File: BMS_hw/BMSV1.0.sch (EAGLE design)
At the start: 237 parts, among them IC1 MC33771BEP, IC2 SFH6156, IC3 MIC28515V1, IC4 FOD8384-COC, IC5 FOD8384-COC, IC6 FOD8384-COC, J2 NTC, Q1 IRLML5203, Q2 IRLML5203, T1 IPT020N10N3V1, T2 IPT020N10N3V1, T3 IPT020N10N3V1, T4 IPT020N10N3V1, X1 87758-2016, X2 87758-1816, X3 22-23-2041, X4 87758-2016, X5 22-23-2051

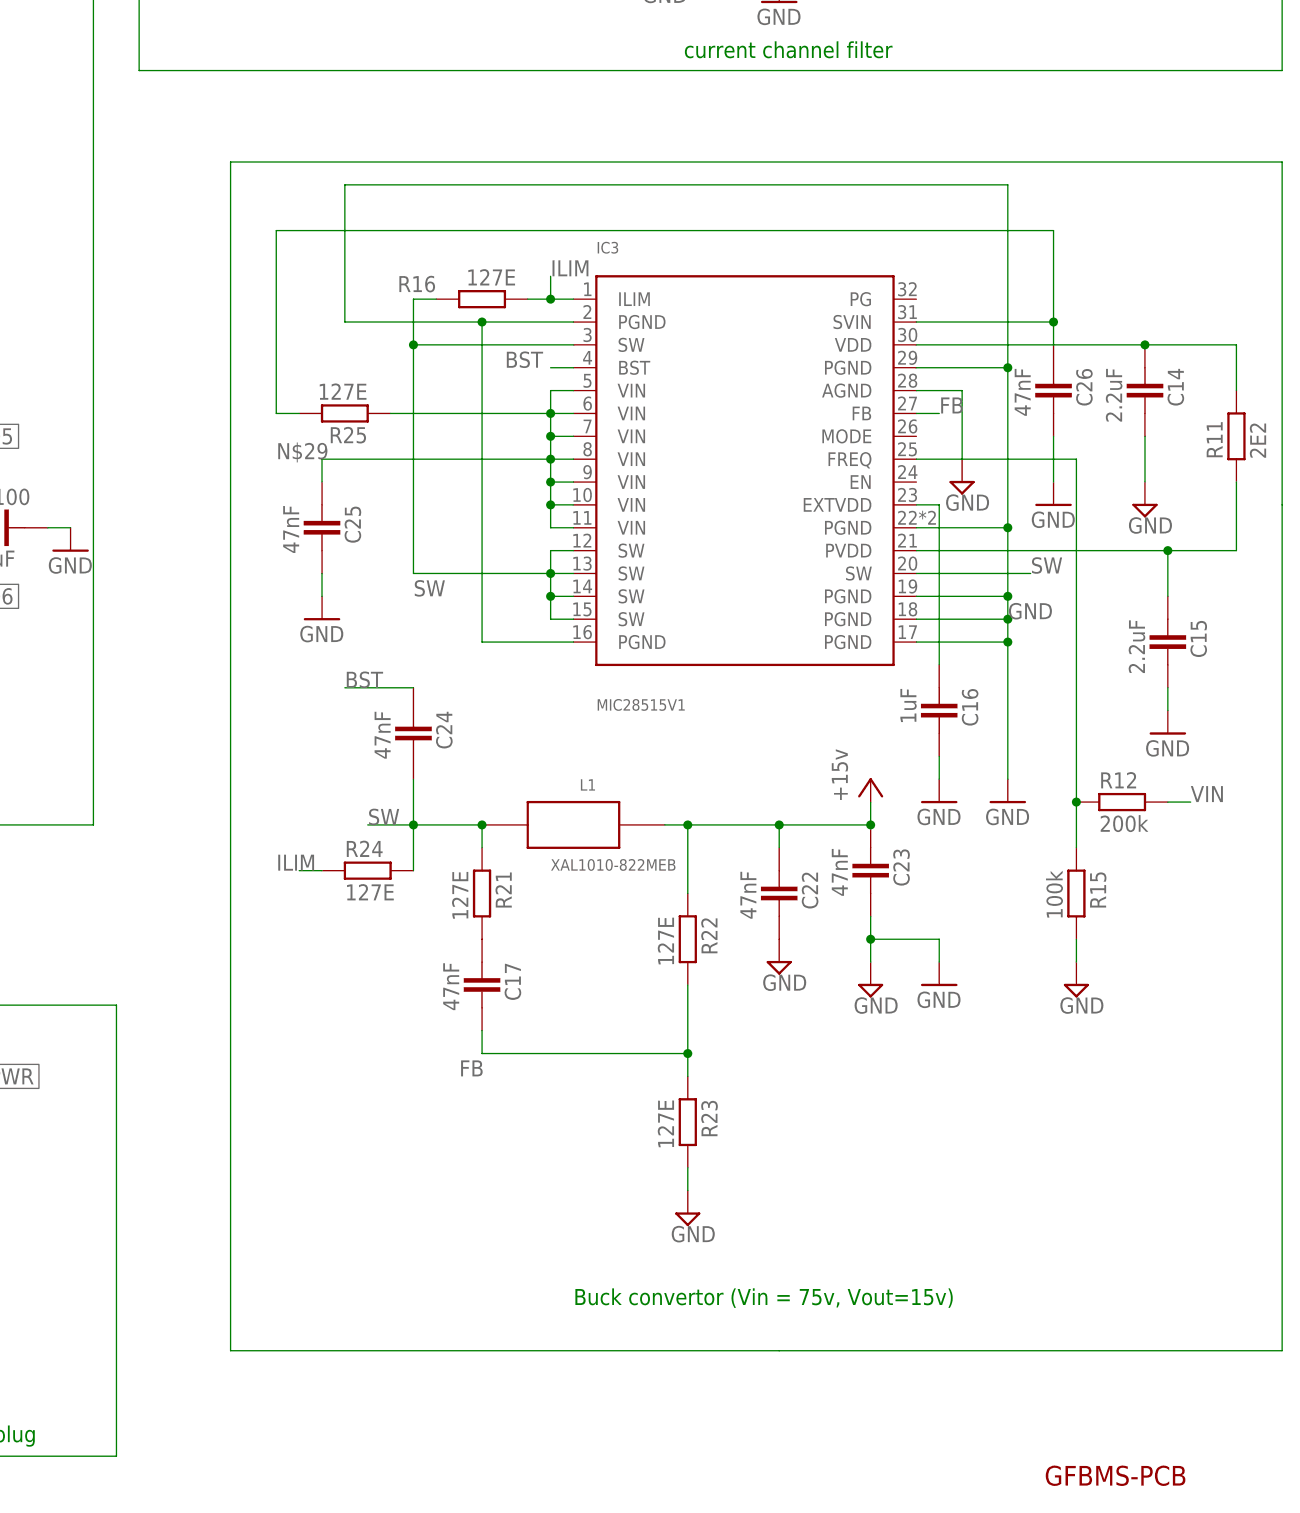
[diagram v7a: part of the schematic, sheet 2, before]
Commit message: afe block placement completed , buck convertor routing 90% done !
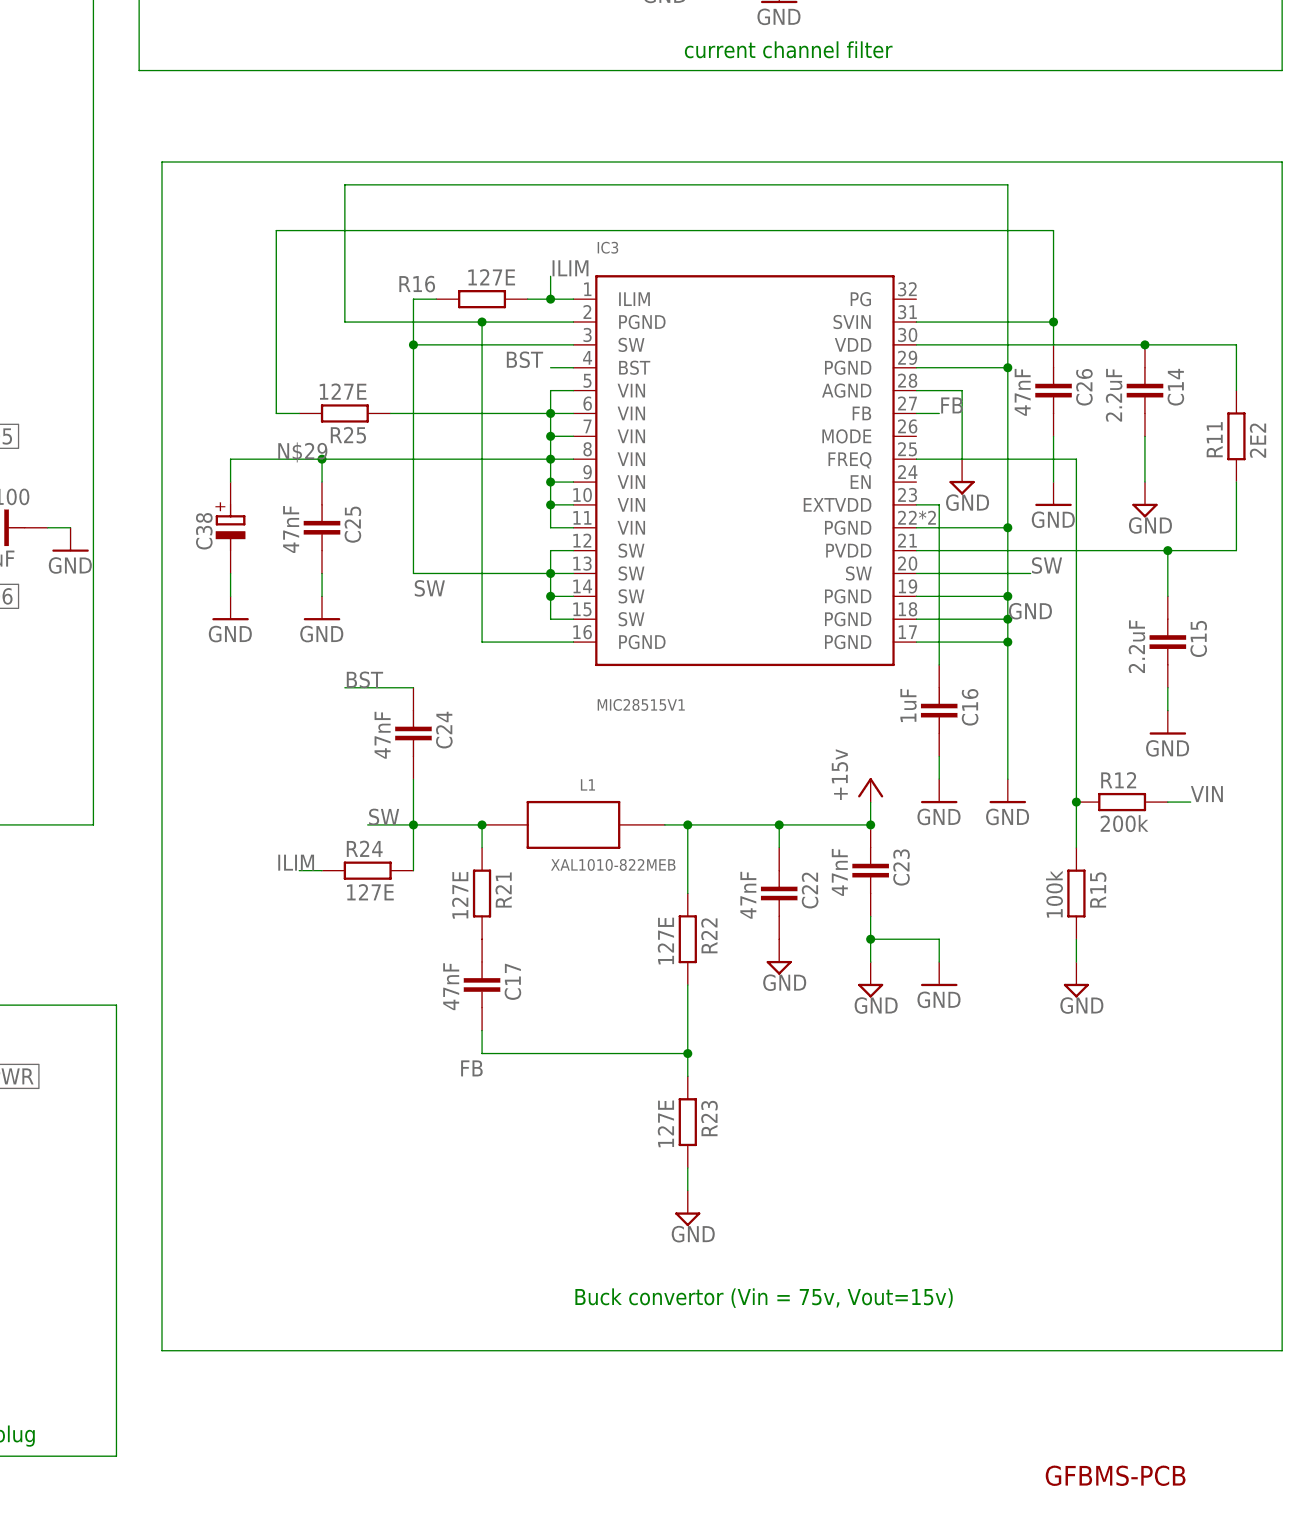
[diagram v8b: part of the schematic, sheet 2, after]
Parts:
- added C38: (no value), ipc-7351-capacitor:POLARISED_CASE_E
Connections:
- net GND: now also C38.-
- net N$29: now also C38.+
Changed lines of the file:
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@@
 <part name="X3" library="GreenFuel" deviceset="22-23-2041" device=""/>
 <part name="X5" library="GreenFuel" deviceset="22-23-2051" device=""/>
+<part name="C38" library="ipc-7351-capacitor" deviceset="POLARISED_" device="CASE_E"/>
+<part name="GND40" library="supply1" library_urn="urn:adsk.eagle:library:371" deviceset="GND" device=""/>
 </parts>
 <sheets>
@@
 <attribute name="VALUE" x="292.1" y="223.52" size="1.778" layer="96" rot="R90"/>
 </instance>
+<instance part="C38" gate="G$1" x="254" y="127" rot="R90">
+<attribute name="NAME" x="251.968" y="124.46" size="1.778" layer="95" rot="R90"/>
+<attribute name="VALUE" x="257.81" y="124.46" size="1.778" layer="96" rot="R90"/>
+</instance>
+<instance part="GND40" gate="1" x="254" y="116.84">
+<attribute name="VALUE" x="251.46" y="114.3" size="1.778" layer="96"/>
+</instance>
 </instances>
 <busses>
@@
 <wire x1="269.24" y1="238.76" x2="269.24" y2="236.22" width="0.1524" layer="91"/>
 </segment>
+<segment>
+<pinref part="GND40" gate="1" pin="GND"/>
+<pinref part="C38" gate="G$1" pin="-"/>
+<wire x1="254" y1="119.38" x2="254" y2="121.92" width="0.1524" layer="91"/>
+</segment>
 </net>
 <net name="N$41" class="0">
@@
 <net name="N$22" class="0">
 <segment>
-<wire x1="254" y1="167.64" x2="370.84" y2="167.64" width="0.1524" layer="91"/>
-<wire x1="370.84" y1="167.64" x2="370.84" y2="129.54" width="0.1524" layer="91"/>
-<wire x1="370.84" y1="129.54" x2="370.84" y2="35.56" width="0.1524" layer="91"/>
-<wire x1="370.84" y1="35.56" x2="314.96" y2="35.56" width="0.1524" layer="91"/>
-<wire x1="314.96" y1="35.56" x2="254" y2="35.56" width="0.1524" layer="91"/>
-<wire x1="254" y1="35.56" x2="254" y2="167.64" width="0.1524" layer="91"/>
+<wire x1="246.38" y1="167.64" x2="370.84" y2="167.64" width="0.1524" layer="91"/>
+<wire x1="370.84" y1="167.64" x2="370.84" y2="35.56" width="0.1524" layer="91"/>
+<wire x1="370.84" y1="35.56" x2="246.38" y2="35.56" width="0.1524" layer="91"/>
+<wire x1="246.38" y1="35.56" x2="246.38" y2="167.64" width="0.1524" layer="91"/>
 </segment>
 </net>
@@
 <wire x1="271.78" y1="139.7" x2="289.56" y2="139.7" width="0.1524" layer="91"/>
 <label x="259.08" y="134.62" size="1.778" layer="95"/>
+<pinref part="C38" gate="G$1" pin="+"/>
+<wire x1="254" y1="132.08" x2="254" y2="134.62" width="0.1524" layer="91"/>
+<wire x1="254" y1="134.62" x2="264.16" y2="134.62" width="0.1524" layer="91"/>
+<junction x="264.16" y="134.62"/>
 </segment>
 </net>
